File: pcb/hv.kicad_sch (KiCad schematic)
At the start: 19 parts, among them Q1 DMN3404L

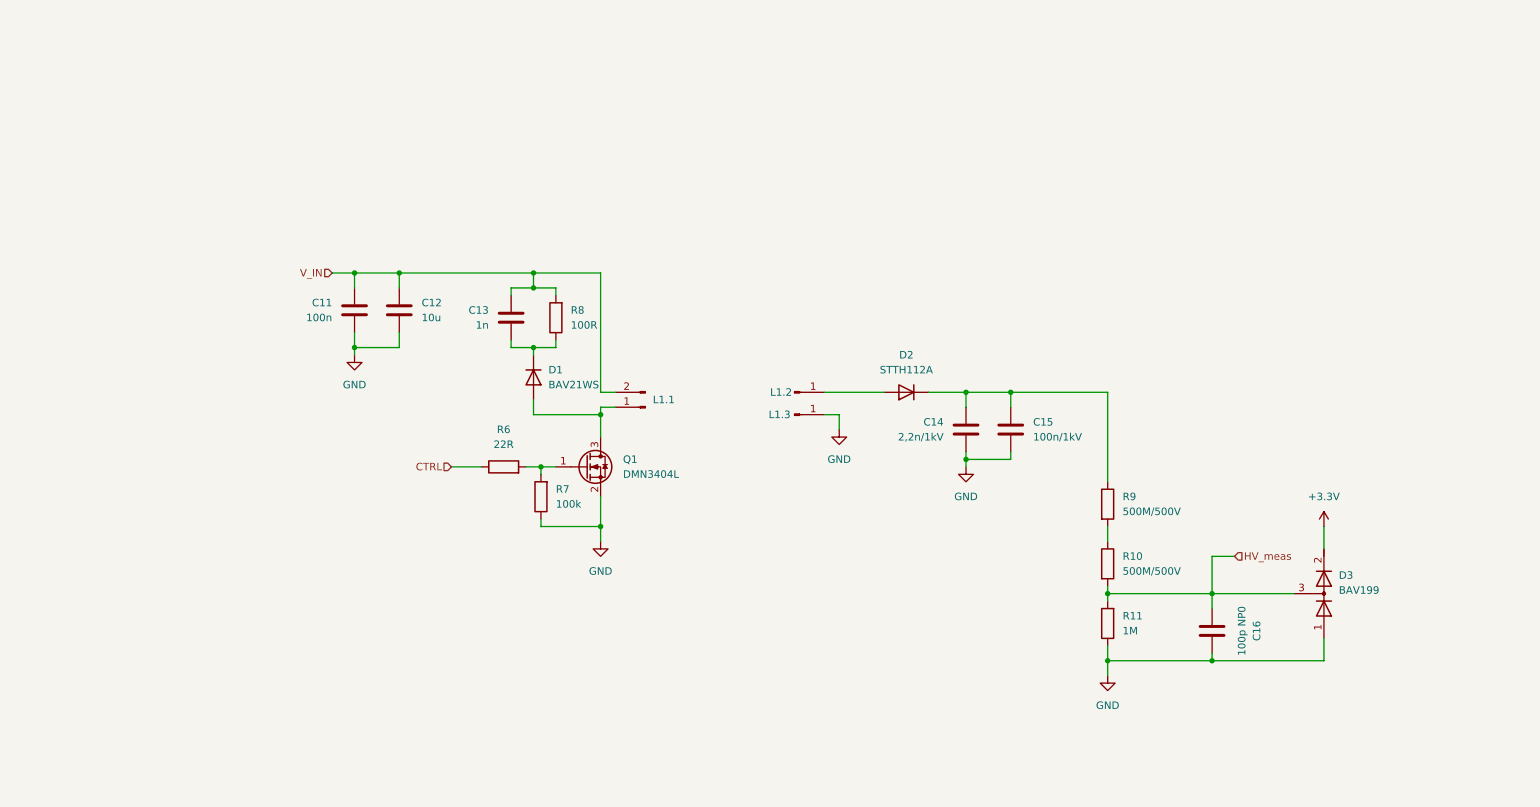
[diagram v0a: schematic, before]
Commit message: Sch almost done, maybe add current sense
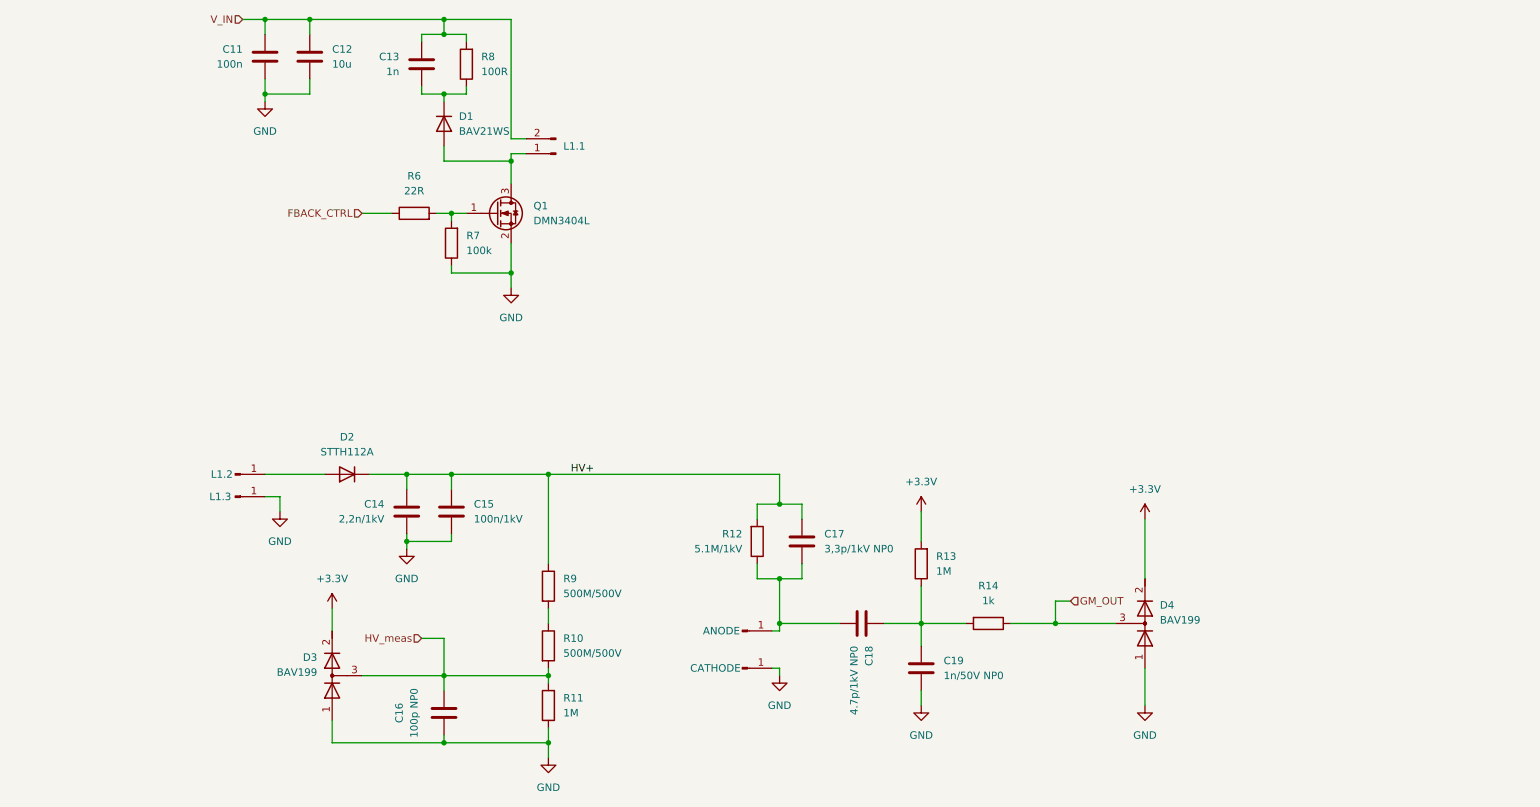
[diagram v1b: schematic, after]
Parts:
- added ANODE, CATHODE: Conn_01x01_Pin, Connector_PinHeader_2.00mm:PinHeader_1x01_P2.00mm_Vertical, symbol Connector:Conn_01x01_Pin
- added C17: 3,3p/1kV NP0, Capacitor_SMD:C_1206_3216Metric, symbol Device:C
- added C18: 4.7p/1kV NP0, Capacitor_SMD:C_1206_3216Metric, symbol Device:C
- added C19: 1n/50V NP0, Capacitor_SMD:C_1206_3216Metric, symbol Device:C
- added D4: BAV199, Package_TO_SOT_SMD:TSOT-23, symbol Device:D_Dual_Series_AKC
- added R12: 5.1M/1kV, Resistor_SMD:R_1206_3216Metric, symbol Device:R
- added R13: 1M, Resistor_SMD:R_0603_1608Metric, symbol Device:R
- added R14: 1k, Resistor_SMD:R_0603_1608Metric, symbol Device:R
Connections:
- net +3.3V: now also D4.2 (K), R13.2
- net GND: now also C19.2, CATHODE.1 (Pin_1), D4.1 (A)
- net HV+: now reaches C14.1, C15.1, D2.1 (K), R9.1
- net HV+: now also C17.1, R12.2
- net CTRL renamed FBACK_CTRL
- new net: C18.1, C19.1, R13.1, R14.2
- new net: ANODE.1 (Pin_1), C17.2, C18.2, R12.1
- new net GM_OUT: D4.3 (common), R14.1
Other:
- moved on the sheet: C11, C12, C13, C14, C15, C16, D1, D2, D3, L1.1, L1.2, L1.3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

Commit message: Scheamtic almost finished, astarted firmware and pcb
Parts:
- renumbered ANODE to ANODE1, CATHODE to CATHODE1
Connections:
- net GM_OUT renamed COMP_GM
- net V_IN renamed +5V
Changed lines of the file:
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@@
 		)
 	)
-	(hierarchical_label "GM_OUT"
-		(shape input)
+	(hierarchical_label "COMP_GM"
+		(shape output)
 		(at 201.93 127 0)
 		(effects
@@
 	)
 	(hierarchical_label "HV_meas"
-		(shape input)
+		(shape output)
 		(at 91.44 133.35 180)
 		(effects
@@
 		)
 	)
-	(hierarchical_label "V_IN"
+	(hierarchical_label "+5V"
 		(shape input)
 		(at 60.96 27.94 180)
@@
 		(in_pos_files yes)
 		(dnp no)
-		(property "Reference" "CATHODE"
+		(property "Reference" "CATHODE1"
 			(at 141.478 138.43 0)
 			(show_name no)
@@
 			(project "geiger_probe"
 				(path "/eb6e66b6-2df0-4872-8f92-4c510b34f8fe/88eb76e9-c2ae-4982-8eef-c2fa556b1d90"
-					(reference "CATHODE")
+					(reference "CATHODE1")
 					(unit 1)
 				)
@@
 		(in_pos_files yes)
 		(dnp no)
-		(property "Reference" "ANODE"
+		(property "Reference" "ANODE1"
 			(at 142.494 132.08 0)
 			(show_name no)
@@
 			(project "geiger_probe"
 				(path "/eb6e66b6-2df0-4872-8f92-4c510b34f8fe/88eb76e9-c2ae-4982-8eef-c2fa556b1d90"
-					(reference "ANODE")
-					(unit 1)
-				)
+					(reference "ANODE1")
+					(unit 1)
+				)

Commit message: Schematic finished, first routing
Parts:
- added F2, F3: 01020071Z, 01020071Z, symbol SamacSys_Parts:01020071Z
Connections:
- net GND: now also F3.1, F3.2
- net at ANODE1.1 (Pin_1), C17.2, C18.2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: now also F2.1, F2.2
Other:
- moved on the sheet: ANODE1, C17, C18, C19, CATHODE1, D4, R12, R13, R14

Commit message: Routing almost finished
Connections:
- net HV+_mid_meas: now reaches R10.1, R9.2
- net HV+_tube: now reaches ANODE1.1 (Pin_1), C17.2, C18.2, F2.1, F2.2, R12.1
- net HV+_L: now reaches D2.2 (A), L1.2.1 (Pin_1)
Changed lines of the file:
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@@
+		)
+	)
+	(label "HV+_L"
+		(at 67.31 105.41 0)
+		(effects
+			(font
+				(size 1.27 1.27)
+			)
+			(justify left bottom)
+		)
+	)
+	(label "HV+_tube"
+		(at 172.72 128.27 0)
+		(effects
+			(font
+				(size 1.27 1.27)
+			)
+			(justify left bottom)
 		)
 	)
@@
 		(effects
 			(font
+				(size 1.27 1.27)
+			)
+			(justify left bottom)
+		)
+	)
+	(label "HV+_mid_meas"
+		(at 113.03 129.54 0)
+		(effects
+			(font

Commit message: Cleaning
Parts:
- added ANODE2: Conn_01x01_Pin, Connector_PinHeader_2.00mm:PinHeader_1x01_P2.00mm_Vertical, symbol Connector:Conn_01x01_Pin
- ANODE1, CATHODE1, F2, F3, L1.1, L1.2, L1.3: now left out of the parts list
- C14, C19: Manufacturer_Part_Number (none) -> CC1206KKX7RC222
- C15: Manufacturer_Part_Number (none) -> GRM43DR7LW104KW01L
- C16: Manufacturer_Part_Number (none) -> 0603N100J500CT
- D1: Manufacturer_Part_Number (none) -> BAV21WS
- D2: Manufacturer_Part_Number (none) -> STTH112A
- D3, D4: Manufacturer_Part_Number (none) -> BAV199
- Q1: Manufacturer_Part_Number (none) -> DMN3404L
- R10, R12, R9: Manufacturer_Part_Number (none) -> HVC1206T5005JET
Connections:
- net HV+_tube: no longer F2.1, F2.2
- new net: ANODE2.1 (Pin_1), F2.1, F2.2

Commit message: Cleaning
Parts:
- removed ANODE2: Conn_01x01_Pin, Connector_PinHeader_2.00mm:PinHeader_1x01_P2.00mm_Vertical, symbol Connector:Conn_01x01_Pin
- removed F2: 01020071Z, 01020071Z, symbol SamacSys_Parts:01020071Z
- F3: footprint 01020071Z -> SamacSys_Parts:01020071Z

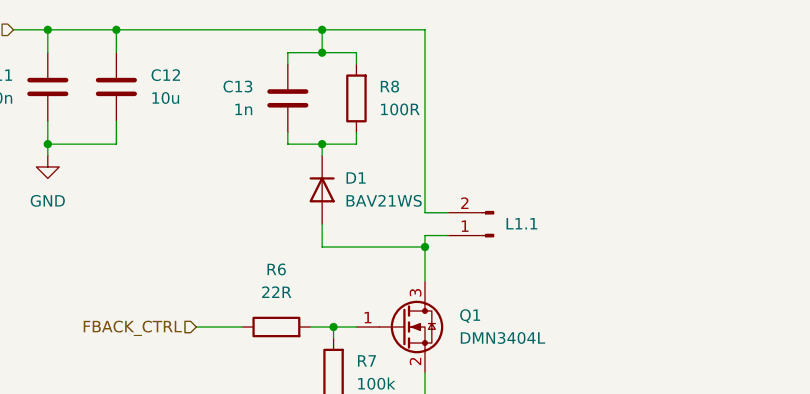
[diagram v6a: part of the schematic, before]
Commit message: Unify resistor/capacitor values and footprints, add via-in-pad DRC rule, regenerate outputs
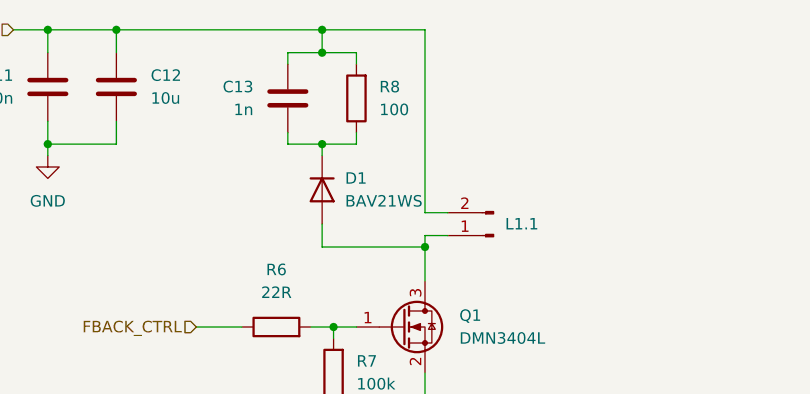
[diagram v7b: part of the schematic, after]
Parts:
- R8: value 100R -> 100
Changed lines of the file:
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@@
 			)
 		)
-		(property "Value" "100R"
+		(property "Value" "100"
 			(at 101.6 36.8299 0)
 			(show_name no)

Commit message: Add J1 net labels and fiducials, regenerate production outputs
- Named nets on J1 pads (schematic + PCB)
- 2 fiducials for stencil alignment (hand assembly)
- Regenerate PDFs, gerber zip, interactive BOM and 3D renders
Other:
- note added: "Geiger Tube Mount"
- note added: "HV transformer"
- moved on the sheet: ANODE1, C11, C12, C13, C14, C15, C16, C17, C18, C19, CATHODE1, D1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
